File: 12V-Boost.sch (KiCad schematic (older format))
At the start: 17 parts, among them J201 Conn_01x03, Q201 BSS214NW, U201 TPS55340-Q1

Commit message: Fixed GPIO 13, GPIO 16 and GPIO 17 for the fan control.
Signed-off-by: Aaron Williams <aaron.w2@gmail.com>
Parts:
- J201: MFR (none) -> -; MPN (none) -> -; SPN (none) -> -; SPR (none) -> -; SPURL (none) -> -

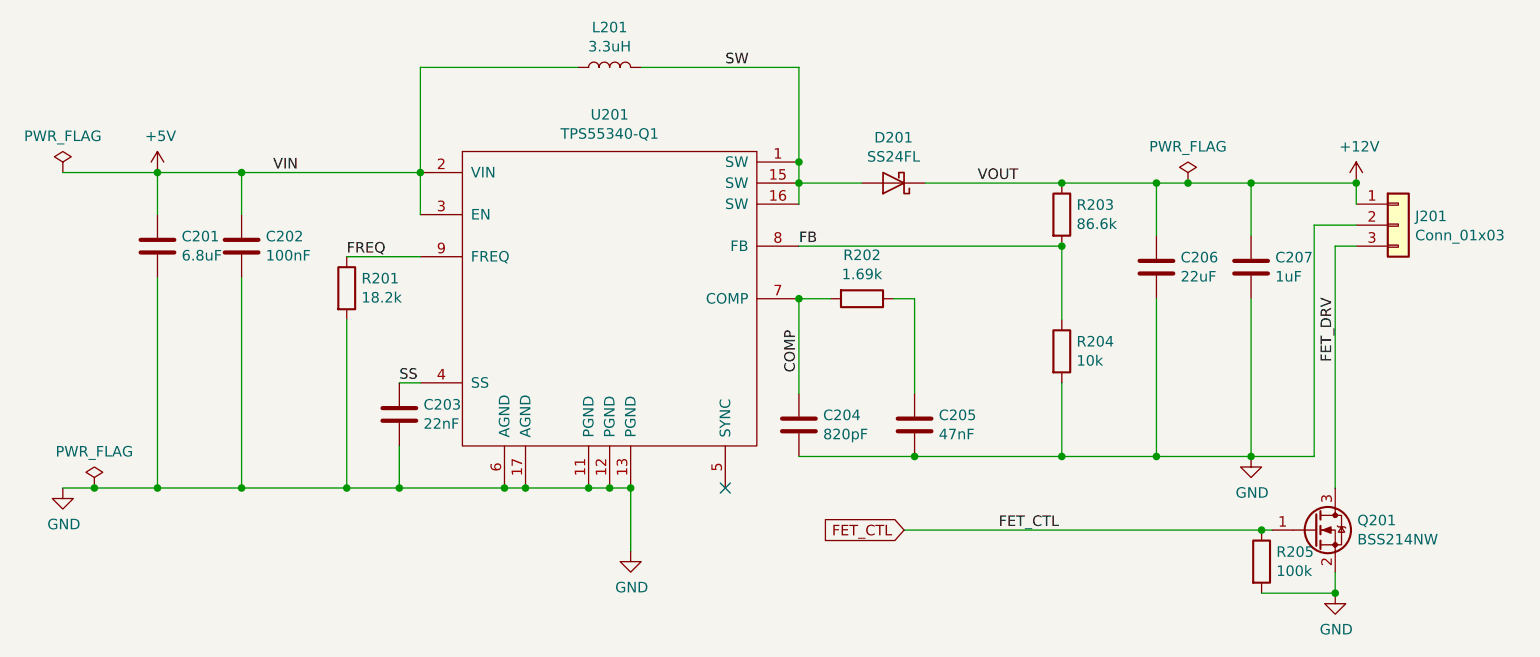
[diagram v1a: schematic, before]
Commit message: Changed GPIOs for Teensy 4.0
The 5V GPIOs were changed for the Teensy 4.0.  In addition the GPIOs to
the 14 pin header were also changed.

Some component values were also changed for the power supply.

Note that this is still compatible with the 3.1 stencil.

This also fixes the 12V BOM.

Signed-off-by: Aaron Williams <aaron.w2@gmail.com>
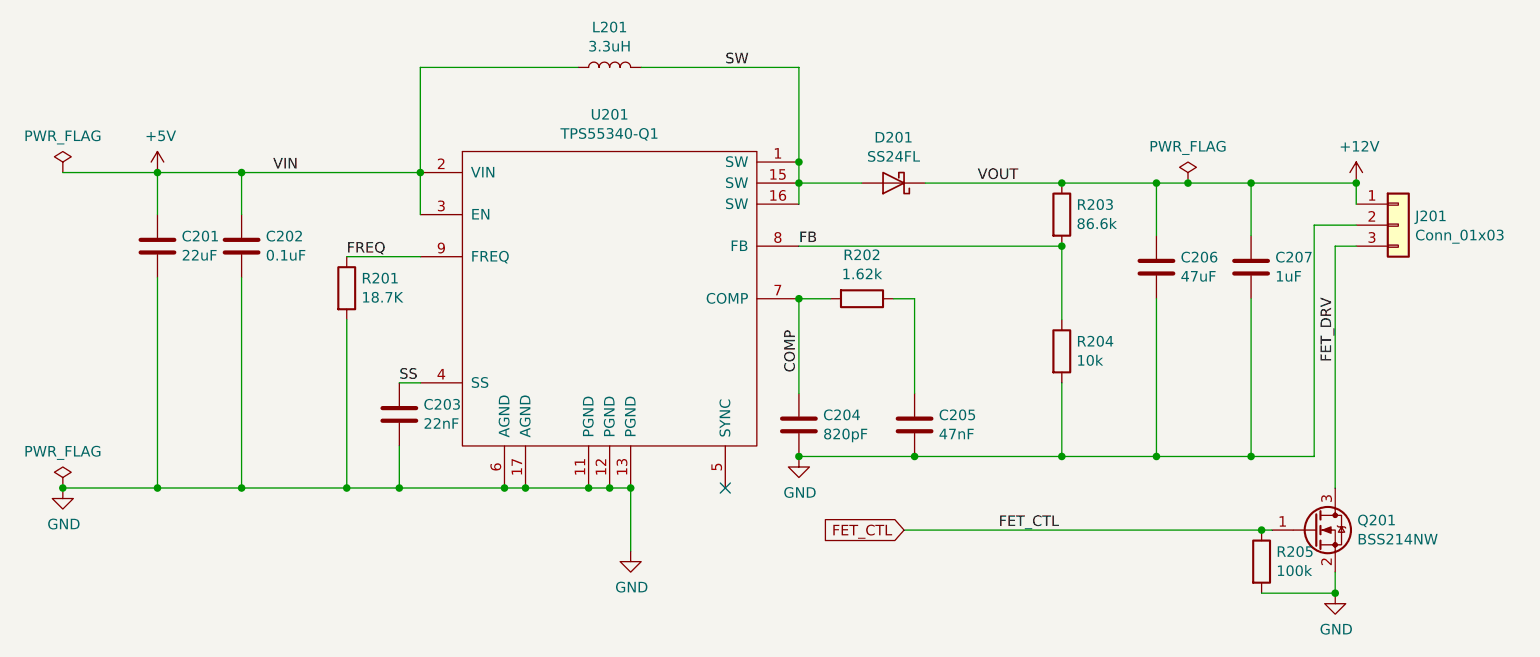
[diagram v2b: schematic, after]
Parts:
- C201: value 6.8uF -> 22uF; DESC (none) -> CAP CER 22UF 16V X5R 0603; MFR TDK -> Samsung Electro-Mechanics; MPN C1608X5R1E685K080AC -> CL10A226MO7JZNC; SPN 445-14145-1-ND -> 1276-7076-1-ND; SPURL - -> https://www.digikey.com/products/en?keywords=1276-7076-1-ND
- C202: value 100nF -> 0.1uF; DESC (none) -> CAP CER 0.1UF 16V X7R 0603; SPURL - -> https://www.digikey.com/products/en?keywords=1276-6582-1-ND
- C203: DESC (none) -> CAP CER 0.022UF 50V X7R 0603; SPURL - -> https://www.digikey.com/products/en?keywords=1276-6534-1-ND
- C204: DESC (none) -> CAP CER 820PF 50V X7R 0603; SPURL - -> https://www.digikey.com/products/en?keywords=399-9127-1-ND
- C205: DESC (none) -> CAP CER 0.047UF 50V X7R 0603; MFR Murata -> Samsung Electro-Mechanics; MPN GRM188R61H474KA12D -> CL10B473KB8WPNC; SPN 490-11994-1-ND -> 1276-6540-1-ND; SPURL - -> https://www.digikey.com/product-detail/en/samsung-electro-m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
- C206: value 22uF -> 47uF; DESC (none) -> CAP CER 47UF 16V X5R 1210; MPN CL32B226MOJNNNE -> CL32A476KOJNNNE; SPN 1276-3395-1-ND -> 1276-3376-1-ND; SPURL - -> https://www.digikey.com/product-detail/en/samsung-electro-m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
- C207: DESC (none) -> CAP CER 1UF 25V X7R 0603; MPN CL10B105KP8NNNC -> CL10B105KA8NNNC; SPN 1276-1946-1-ND -> 1276-1184-1-ND; SPURL - -> https://www.digikey.com/products/en?keywords=1276-1184-1-ND
- D201: DESC (none) -> DIODE SCHOTTKY 40V 2A SOD123F; SPURL - -> https://www.digikey.com/products/en?keywords=SS24FLCT-ND
- J201: DESC (none) -> -
- L201: DESC (none) -> FIXED IND 3.3UH 2.7A 61 MOHM SMD; SPURL - -> https://www.digikey.com/product-detail/en/IHLP1212BZER3R3M1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
- Q201: DESC (none) -> MOSFET N-CH 20V 1.5A SOT323; SPURL - -> https://www.digikey.com/products/en?keywords=BSS214NWH6327X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
- R201: value 18.2k -> 18.7K; DESC (none) -> RES SMD 18.7K OHM 1% 1/10W 0603; MFR Vishay Dale -> Yageo; MPN CRCW060318K2FKEA -> RC0603FR-0718K7L; SPN 541-18.2KHCT-ND -> 311-18.7KHRCT-ND; SPURL - -> https://www.digikey.com/product-detail/en/yageo/RC0603FR-07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
- R202: value 1.69k -> 1.62k; DESC (none) -> RES SMD 1.62K OHM 1% 1/10W 0603; MFR Vishay -> Yageo; MPN CRCW06031K69FKEA -> RC0603FR-071K62L; SPN 541-1.69KHCT-ND -> 311-1.62KHRCT-ND; SPURL - -> https://www.digikey.com/product-detail/en/yageo/RC0603FR-07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
- R203: DESC (none) -> RES SMD 86.6K OHM 1% 1/10W 0603; SPURL - -> https://www.digikey.com/products/en?keywords=541-86.6KHCT-ND
- R204: DESC (none) -> RES SMD 10K OHM 1% 1/10W 0603; SPURL - -> https://www.digikey.com/products/en?keywords=541-2979-1-ND
- R205: DESC (none) -> RES SMD 100K OHM 1% 1/10W 0603; SPURL - -> https://www.digikey.com/products/en?keywords=A106046CT-ND
- U201: DESC (none) -> IC REG BOOST ADJ 5.25A 16WQFN; SPURL - -> https://www.digikey.com/products/en?keywords=296-37677-1-ND

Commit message: Added pull-up resistors to 14-pin header
Made board 4 layers

Made board double sided

Signed-off-by: Aaron Williams <aaron.w2@gmail.com>
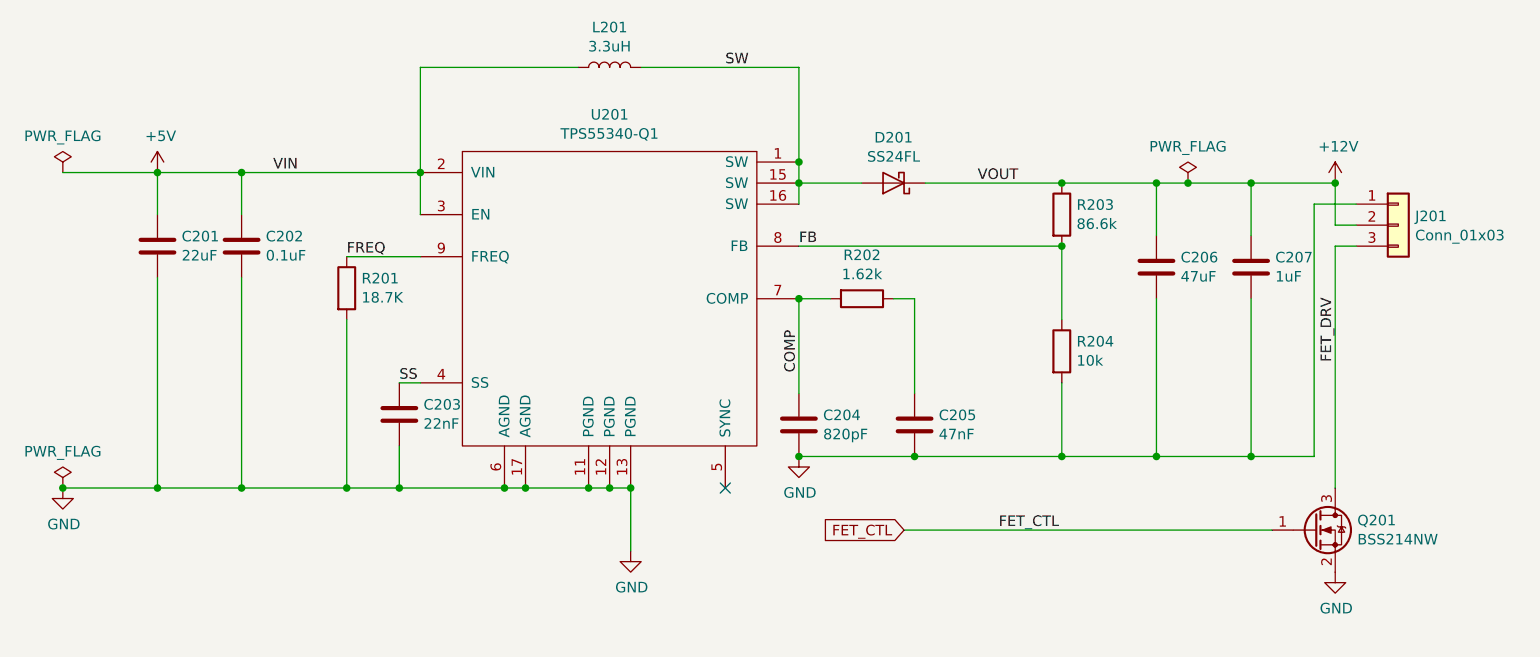
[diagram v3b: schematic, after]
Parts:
- removed R205: 100k, Resistor_SMD:R_0603_1608Metric, symbol Device:R
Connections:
- net +12V: now also J201.2 (Pin_2); no longer J201.1 (Pin_1)
- net GND: now also J201.1 (Pin_1); no longer J201.2 (Pin_2)
